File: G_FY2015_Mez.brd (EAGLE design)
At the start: 160 x 100 mm, 203 parts, among them IC100 FT232RL, IC101 FT245RL, J100 EPL.00.250.NTN, J110 EPL.00.250.NTN, J120 EPL.00.250.NTN, J121 IL-2P-S3EN2, J130 EPL.00.250.NTN, J131 IL-2P-S3EN2, J180 TOKUDEN_SP6, J181 USB Mini-B Connector, J182 USB Mini-B Connector, J300 SHV_PIGTAIL_LAND, J301 SHV_PIGTAIL_LAND, J400 RPI2_GPIO_HOLES, J410 IL-3P-S3EN2, J411 IL-3P-S3EN2, J600_12V IL-4P-S3EN2, J610 2.1MMJACKTHM, J620 IL-2P-S3EN2, J630 USB_TYPEA_LUMBERG_2410_01, J640 USB_TYPEA_LUMBERG_2410_01, J650_VOUT IL-4P-S3EN2, U100 AD9215LONG_PAD, U101 AD8138, U102 LM6172, U110 AD9215LONG_PAD, U111 AD8138, U112 LM6172, U120 AD9215LONG_PAD, U121 AD8138, U130 AD9215LONG_PAD, U131 AD8138, U191 GPS_FGPMMOPA6H, U300 OPTON_1PA_12, U301 OPTON_1PA_12, U302 2SC1815, U303 2SJ681, U410 MCP3208-CI/SL, U411 MCP1525TSOT-23-3, U412 LM60, U413 LM60, U500 LT6106, U510 LT6106, U520 2SC1815, U521 2SJ681, U600 PHT12050WAH, U610 PHT12050WAH, U620 LTC1983ES6-3, U621 LTC1983ES6-5

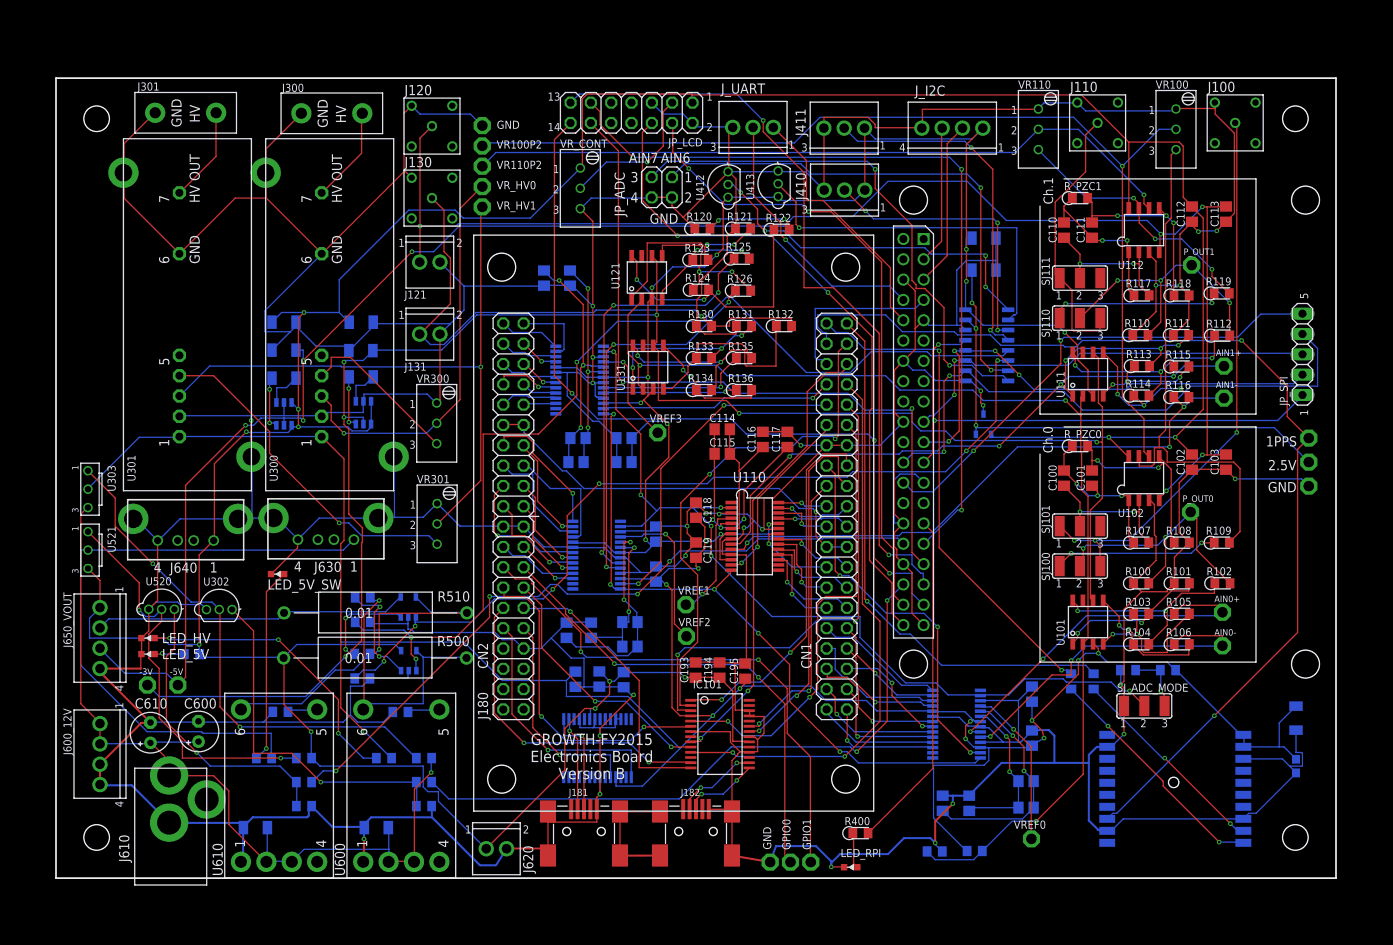
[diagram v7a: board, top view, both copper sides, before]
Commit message: netclass "power" added, and supply/gnd signals changed to "power" net
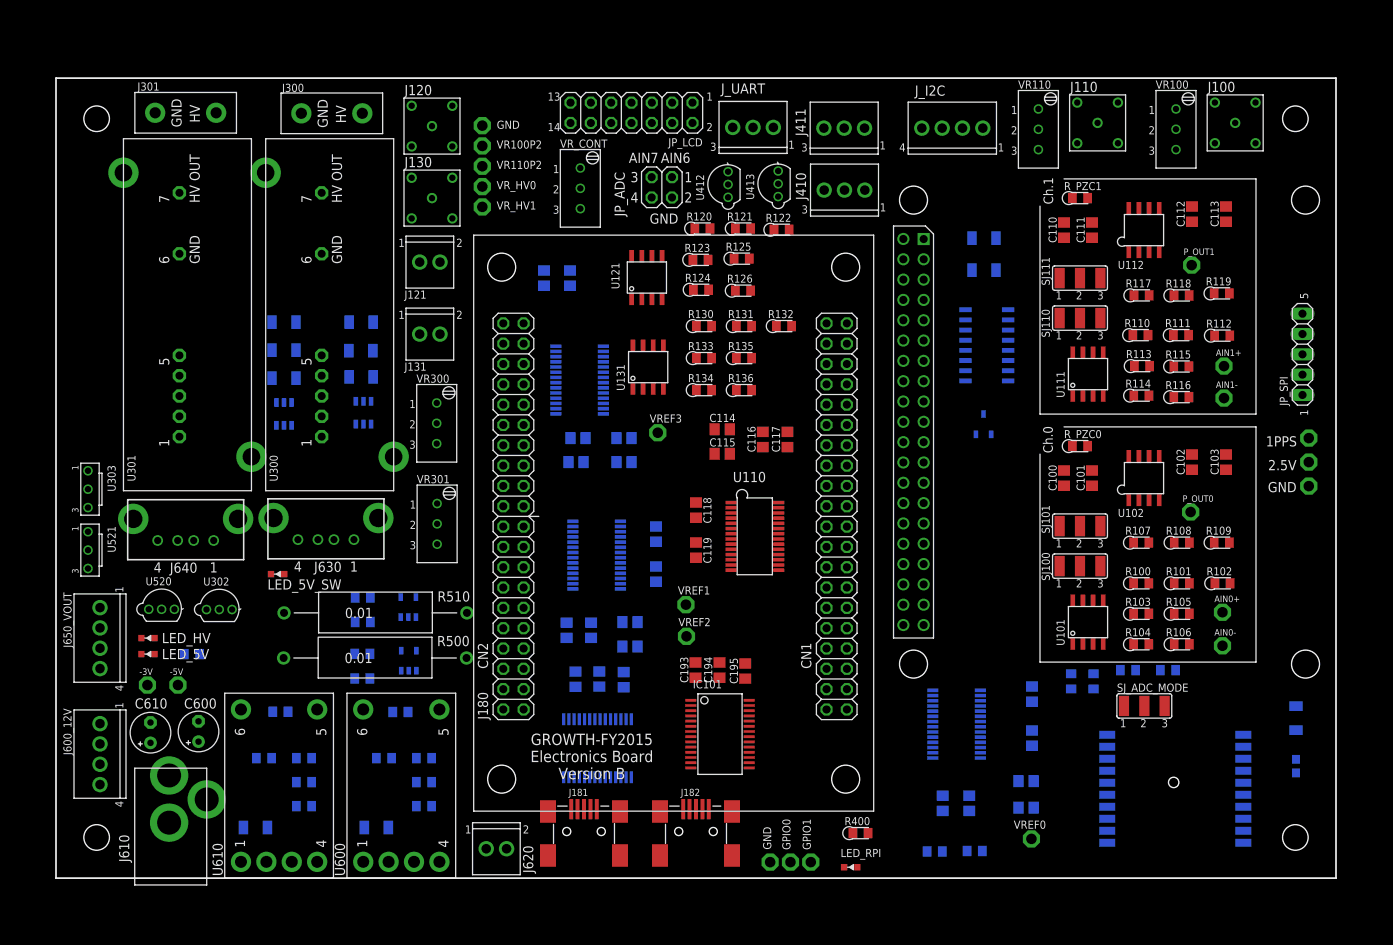
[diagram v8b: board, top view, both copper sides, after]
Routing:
- net GND: track 1308.8 -> 0.00 mm, vias 27 -> 0
- net +3V3: track 487.4 -> 0.00 mm, vias 22 -> 0
- net +5V: track 432.9 -> 0.00 mm, vias 11 -> 0
- net -5V: track 238.8 -> 0.00 mm, vias 8 -> 0
- net -3V3: track 220.1 -> 0.00 mm, vias 6 -> 0
- net ADC_CM: track 143.1 -> 0.00 mm, vias 3 -> 0
- net GPS_1PPS: track 133.3 -> 0.00 mm, vias 2 -> 0
- net N$73: track 130.4 -> 0.00 mm, vias 1 -> 0
- net SLOWADC_4: track 125.6 -> 0.00 mm, vias 3 -> 0
- net ADC_MODE: track 110.4 -> 0.00 mm, vias 6 -> 0
- net +12V: track 109.5 -> 0.00 mm, vias 1 -> 0
- net SLOWADC_5: track 108.1 -> 0.00 mm, vias 6 -> 0
- net LCD_D7: track 100.5 -> 0.00 mm, vias 3 -> 0
- net LCD_D4: track 99.8 -> 0.00 mm, vias 3 -> 0
- net LCD_D6: track 96.2 -> 0.00 mm, vias 2 -> 0
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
